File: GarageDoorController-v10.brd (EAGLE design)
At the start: 84.8 x 61 mm, 21 parts, among them IC1 ATMEGA328, IC2 TO-220, J1 ICSP, J2 DCJ0202, Q1 2N2222A, X1 Garage Door, X2 Reed Switch, X3 ETH SHLD, X4 ETH SHLD, Y1 16MHz

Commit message: GarageDoorController-v10.brd file should be ready for home fabrication.
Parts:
- moved J1 1.27 mm to (80.0, 25.4)
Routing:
- net +5V: track 150.7 -> 161.1 mm, vias 0 -> 1
- net N$17: track 0.00 -> 8.93 mm
- net N$10: track 0.00 -> 8.89 mm
- net N$9: track 0.00 -> 7.62 mm
- net N$8: track 0.00 -> 6.65 mm
- net GND: vias 0 -> 2
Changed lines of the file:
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@@
 <element name="D1" library="diode" package="DO41-10" value="1N4004" x="25.4" y="45.72"/>
 <element name="Q1" library="transistor-npn" package="TO18" value="2N2222A" x="29.21" y="38.1"/>
-<element name="J1" library="SparkFun-Connectors" package="2X3" value="ICSP" x="81.28" y="25.4" rot="R90"/>
+<element name="J1" library="SparkFun-Connectors" package="2X3" value="ICSP" x="80.01" y="25.4" rot="R90"/>
 <element name="LED1" library="led" package="LED5MM" value="RED" x="62.23" y="8.89" rot="R270"/>
 <element name="J2" library="con-jack" package="DCJ0202" value="DCJ0202" x="8.89" y="7.62" smashed="yes" rot="R270">
@@
 <wire x1="60.96" y1="58.42" x2="59.69" y2="60.325" width="0.6096" layer="16"/>
 <wire x1="59.69" y1="60.325" x2="34.29" y2="58.42" width="0.6096" layer="16"/>
-<wire x1="35.31" y1="58.17" x2="34.29" y2="58.42" width="0" layer="19" extent="16-16"/>
-<wire x1="48.26" y1="21.59" x2="50.8" y2="29.21" width="0" layer="19" extent="1-1"/>
-<wire x1="49.53" y1="4.064" x2="48.26" y2="21.59" width="0" layer="19" extent="1-1"/>
 <wire x1="3.81" y1="39.33" x2="20.32" y2="45.72" width="0.6096" layer="16"/>
 <wire x1="45.72" y1="21.59" x2="48.26" y2="21.59" width="0.6096" layer="16"/>
 <wire x1="50.8" y1="29.21" x2="50.8" y2="31.75" width="0.6096" layer="16"/>
-<wire x1="50.8" y1="31.75" x2="53.34" y2="34.29" width="0.6096" layer="16"/>
+<wire x1="50.8" y1="31.75" x2="52.07" y2="33.02" width="0.6096" layer="16"/>
+<wire x1="52.07" y1="33.02" x2="53.34" y2="34.29" width="0.6096" layer="16"/>
 <wire x1="53.34" y1="34.29" x2="58.42" y2="34.29" width="0.6096" layer="16"/>
+<wire x1="49.53" y1="4.064" x2="49.53" y2="1.27" width="0.6096" layer="16"/>
+<via x="52.07" y="33.02" extent="1-16" drill="1"/>
+<wire x1="48.26" y1="21.59" x2="48.26" y2="13.97" width="0.6096" layer="16"/>
+<wire x1="35.31" y1="58.17" x2="34.29" y2="58.42" width="0" layer="19" extent="16-16"/>
+<wire x1="48.26" y1="21.59" x2="50.8" y2="29.21" width="0" layer="19" extent="1-1"/>
+<wire x1="49.53" y1="4.064" x2="48.26" y2="13.97" width="0" layer="19" extent="16-16"/>
 </signal>
 <signal name="GND">
@@
 <wire x1="52.38" y1="46.68" x2="53.34" y2="45.72" width="0.6096" layer="16"/>
 <wire x1="53.34" y1="45.72" x2="53.34" y2="41.91" width="0.6096" layer="16"/>
-<wire x1="53.34" y1="41.91" x2="48.26" y2="29.21" width="0.6096" layer="16"/>
-<wire x1="50.8" y1="21.59" x2="55.88" y2="12.7" width="0.6096" layer="16"/>
+<wire x1="53.34" y1="41.91" x2="50.8" y2="35.56" width="0.6096" layer="16"/>
+<wire x1="50.8" y1="35.56" x2="48.26" y2="29.21" width="0.6096" layer="16"/>
+<wire x1="50.8" y1="21.59" x2="53.34" y2="17.145" width="0.6096" layer="16"/>
+<wire x1="53.34" y1="17.145" x2="55.88" y2="12.7" width="0.6096" layer="16"/>
 <wire x1="55.88" y1="12.7" x2="62.23" y2="13.97" width="0.6096" layer="16"/>
 <wire x1="62.23" y1="13.97" x2="66.04" y2="12.7" width="0.6096" layer="16"/>
 <wire x1="66.04" y1="12.7" x2="66.13769375" y2="8.1084625" width="0.6096" layer="16"/>
+<via x="50.8" y="35.56" extent="1-16" drill="1"/>
+<via x="53.34" y="17.145" extent="1-16" drill="1"/>
 <wire x1="50.8" y1="21.59" x2="48.26" y2="29.21" width="0" layer="19" extent="1-1"/>
 </signal>
@@
 <contactref element="J1" pad="3"/>
 <contactref element="IC1" pad="19"/>
-<wire x1="43.18" y1="21.59" x2="81.28" y2="27.94" width="0" layer="19" extent="1-1"/>
+<wire x1="80.01" y1="27.94" x2="82.55" y2="29.21" width="0.6096" layer="16"/>
+<wire x1="43.18" y1="21.59" x2="43.18" y2="17.78" width="0.6096" layer="16"/>
+<wire x1="43.18" y1="21.59" x2="80.01" y2="27.94" width="0" layer="19" extent="1-1"/>
 </signal>
 <signal name="N$9">
 <contactref element="J1" pad="1"/>
 <contactref element="IC1" pad="18"/>
-<wire x1="40.64" y1="21.59" x2="81.28" y2="25.4" width="0" layer="19" extent="1-1"/>
+<wire x1="80.01" y1="25.4" x2="80.01" y2="21.59" width="0.6096" layer="16"/>
+<wire x1="40.64" y1="21.59" x2="40.64" y2="17.78" width="0.6096" layer="16"/>
+<wire x1="40.64" y1="21.59" x2="80.01" y2="21.59" width="0" layer="19" extent="16-16"/>
 </signal>
 <signal name="N$10">
 <contactref element="J1" pad="4"/>
 <contactref element="IC1" pad="17"/>
-<wire x1="38.1" y1="21.59" x2="78.74" y2="27.94" width="0" layer="19" extent="1-1"/>
+<wire x1="77.47" y1="27.94" x2="72.39" y2="27.94" width="0.6096" layer="16"/>
+<wire x1="38.1" y1="21.59" x2="38.1" y2="17.78" width="0.6096" layer="16"/>
+<wire x1="38.1" y1="21.59" x2="72.39" y2="27.94" width="0" layer="19" extent="16-16"/>
 </signal>
 <signal name="N$11">
@@
 <contactref element="IC1" pad="16"/>
 <contactref element="X4" pad="2"/>
-<wire x1="35.56" y1="21.59" x2="58.46" y2="57.15" width="0" layer="19" extent="1-1"/>
+<wire x1="35.56" y1="21.59" x2="35.56" y2="17.78" width="0.6096" layer="16"/>
+<wire x1="58.46" y1="57.15" x2="53.34" y2="57.15" width="0.6096" layer="16"/>
+<wire x1="35.56" y1="21.59" x2="53.34" y2="57.15" width="0" layer="19" extent="16-16"/>
+</signal>
+<signal name="N$4">
+<via x="35.56" y="17.78" extent="1-16" drill="1"/>
+</signal>
+<signal name="N$18">
+<via x="38.1" y="17.78" extent="1-16" drill="1"/>
+</signal>
+<signal name="N$19">
+<via x="40.64" y="17.78" extent="1-16" drill="1"/>
+</signal>
+<signal name="N$20">
+<via x="43.18" y="17.78" extent="1-16" drill="1"/>
+</signal>
+<signal name="N$21">
+<via x="48.26" y="17.78" extent="1-16" drill="1"/>
+</signal>
+<signal name="N$22">
+<via x="80.01" y="21.59" extent="1-16" drill="1"/>
+</signal>
+<signal name="N$23">
+<via x="72.39" y="27.94" extent="1-16" drill="1"/>
+</signal>
+<signal name="N$24">
+<via x="82.55" y="29.21" extent="1-16" drill="1"/>
+</signal>
+<signal name="N$25">
+<via x="53.34" y="57.15" extent="1-16" drill="1"/>
+</signal>
+<signal name="N$26">
+<via x="49.53" y="1.27" extent="1-16" drill="1"/>
+</signal>
+<signal name="N$3">
+<via x="48.26" y="13.97" extent="1-16" drill="1"/>
 </signal>
 </signals>

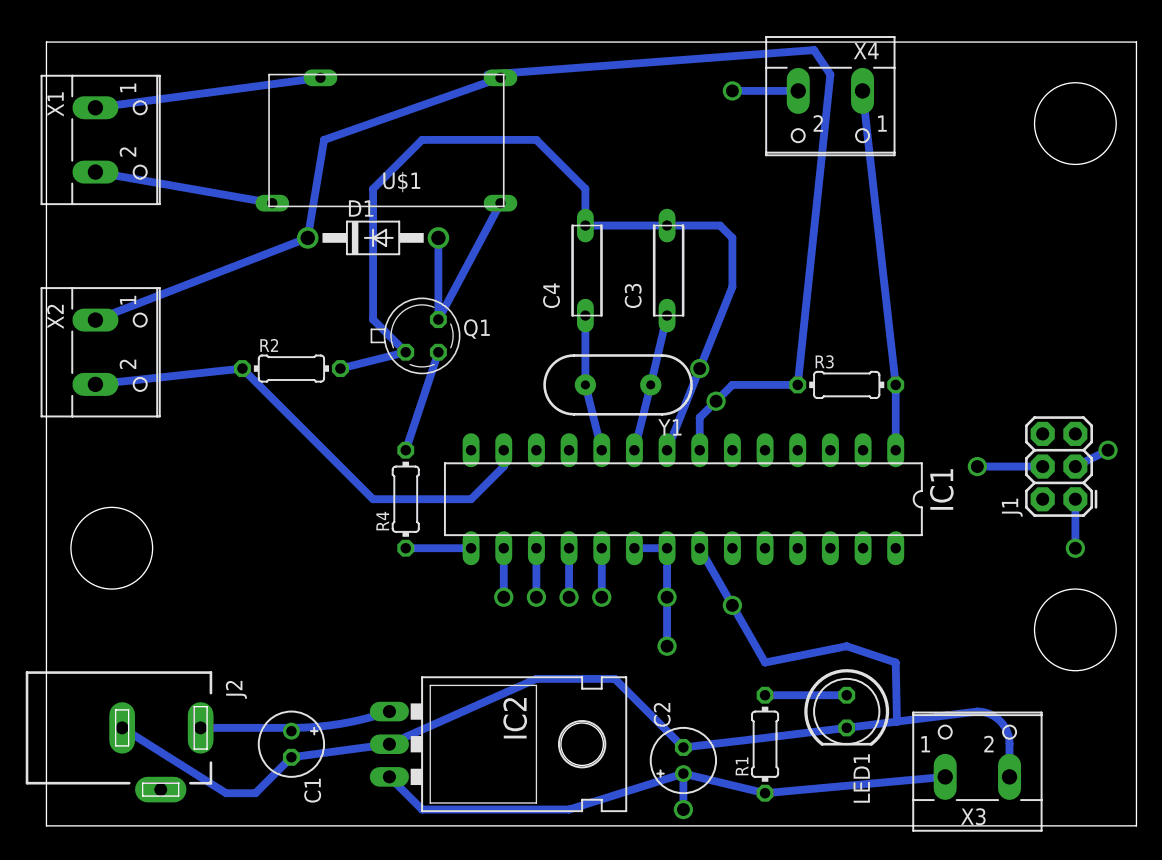
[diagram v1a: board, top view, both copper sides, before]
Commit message: Fixed the pin locations of the relay, added 'Thumbs.db' to .gitignore.
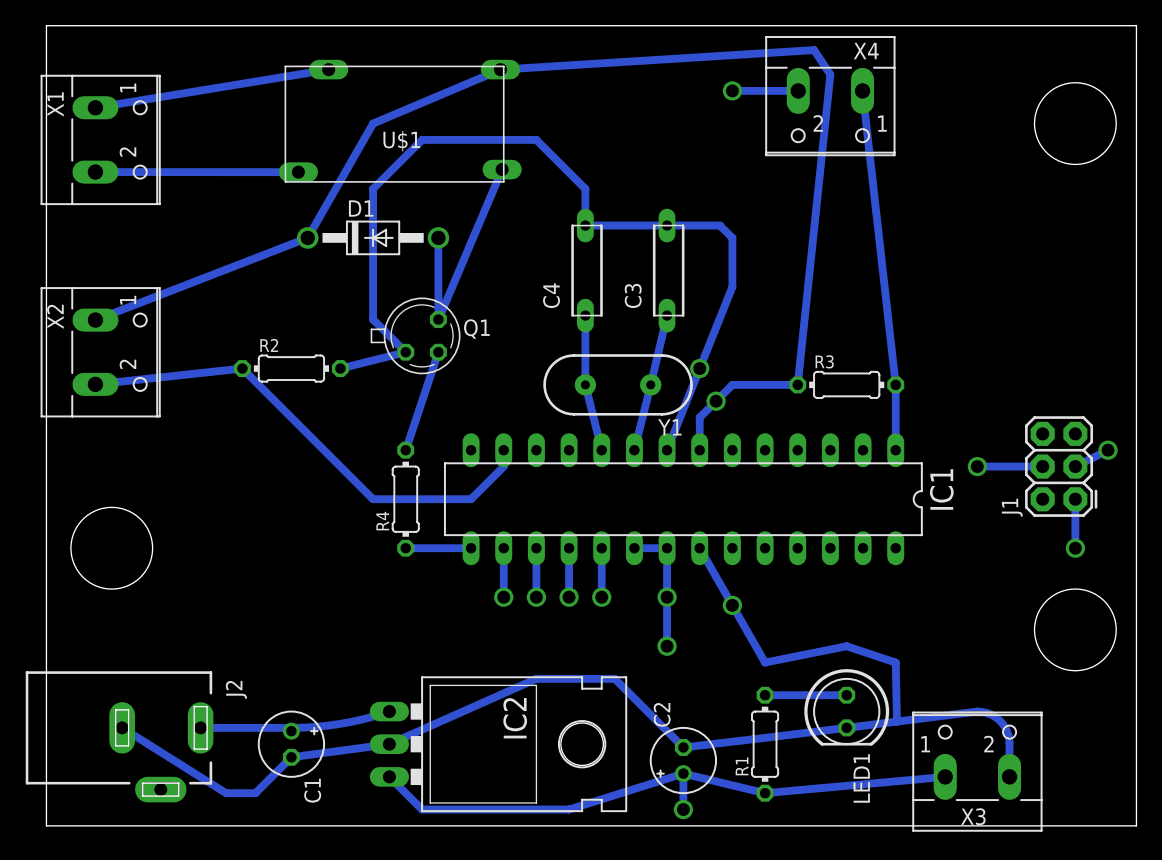
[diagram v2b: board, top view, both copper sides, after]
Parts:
- moved U$1 0.63 mm to (35.6, 59.1)
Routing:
- net N$13: track 16.6 -> 19.0 mm
- net +5V: track 161.1 -> 158.8 mm
- net N$14: track 14.0 -> 15.8 mm
- net N$16: track 17.7 -> 18.4 mm
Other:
- board size 84.8 x 61 mm -> 84.8 x 62.2 mm
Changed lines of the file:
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@@
 <plain>
 <wire x1="0" y1="0" x2="84.76" y2="0" width="0" layer="20"/>
-<wire x1="84.76" y1="0" x2="84.76" y2="60.95" width="0" layer="20"/>
-<wire x1="84.76" y1="60.95" x2="0" y2="60.95" width="0" layer="20"/>
-<wire x1="0" y1="60.95" x2="0" y2="0" width="0" layer="20"/>
+<wire x1="84.76" y1="0" x2="84.76" y2="62.22" width="0" layer="20"/>
+<wire x1="84.76" y1="62.22" x2="0" y2="62.22" width="0" layer="20"/>
+<wire x1="0" y1="62.22" x2="0" y2="0" width="0" layer="20"/>
 <hole x="80.01" y="54.61" drill="6.35"/>
 <hole x="80.01" y="15.24" drill="6.35"/>
@@
 <element name="C3" library="domiflichi" package="1440PH" value="1440PH" x="48.26" y="43.18"/>
 <element name="C4" library="domiflichi" package="1440PH" value="1440PH" x="41.91" y="43.18"/>
-<element name="U$1" library="domiflichi" package="PB874" value="PB874FORMA" x="35.56" y="58.42" rot="R180"/>
+<element name="U$1" library="domiflichi" package="PB874" value="PB874FORMA" x="35.56" y="59.055" rot="R180"/>
 <element name="X3" library="con-wago-500" package="W237-102" value="ETH SHLD" x="72.39" y="5.08" smashed="yes">
 <attribute name="OC_NEWARK" value="70K9898" x="90.17" y="-45.72" size="1.778" layer="27" display="off"/>
@@
 <wire x1="40.64" y1="1.27" x2="49.53" y2="4.064" width="0.6096" layer="16"/>
 <wire x1="49.53" y1="4.064" x2="55.88" y2="2.54" width="0.6096" layer="16"/>
-<wire x1="35.31" y1="58.17" x2="21.59" y2="53.34" width="0.6096" layer="16"/>
-<wire x1="21.59" y1="53.34" x2="20.32" y2="45.72" width="0.6096" layer="16"/>
+<wire x1="25.4" y1="54.61" x2="20.32" y2="45.72" width="0.6096" layer="16"/>
 <wire x1="58.42" y1="34.29" x2="60.96" y2="58.42" width="0.6096" layer="16"/>
 <wire x1="60.96" y1="58.42" x2="59.69" y2="60.325" width="0.6096" layer="16"/>
-<wire x1="59.69" y1="60.325" x2="34.29" y2="58.42" width="0.6096" layer="16"/>
 <wire x1="3.81" y1="39.33" x2="20.32" y2="45.72" width="0.6096" layer="16"/>
 <wire x1="45.72" y1="21.59" x2="48.26" y2="21.59" width="0.6096" layer="16"/>
@@
 <via x="52.07" y="33.02" extent="1-16" drill="1"/>
 <wire x1="48.26" y1="21.59" x2="48.26" y2="13.97" width="0.6096" layer="16"/>
-<wire x1="35.31" y1="58.17" x2="34.29" y2="58.42" width="0" layer="19" extent="16-16"/>
+<wire x1="35.31" y1="58.805" x2="25.4" y2="54.61" width="0.6096" layer="16"/>
 <wire x1="48.26" y1="21.59" x2="50.8" y2="29.21" width="0" layer="19" extent="1-1"/>
 <wire x1="49.53" y1="4.064" x2="48.26" y2="13.97" width="0" layer="19" extent="16-16"/>
+<wire x1="35.31" y1="58.805" x2="59.69" y2="60.325" width="0.6096" layer="16"/>
 </signal>
 <signal name="GND">
@@
 <contactref element="U$1" pad="1"/>
 <wire x1="30.48" y1="45.72" x2="30.48" y2="39.37" width="0.6096" layer="16"/>
-<wire x1="35.31" y1="48.42" x2="30.48" y2="39.37" width="0.6096" layer="16"/>
+<wire x1="35.437" y1="51.03621875" x2="30.48" y2="39.37" width="0.6096" layer="16"/>
 </signal>
 <signal name="N$15">
@@
 <contactref element="U$1" pad="4"/>
 <contactref element="X1" pad="2"/>
-<wire x1="3.81" y1="50.84" x2="17.56" y2="48.42" width="0.6096" layer="16"/>
+<wire x1="3.81" y1="50.84" x2="19.593559375" y2="50.83301875" width="0.6096" layer="16"/>
 </signal>
 <signal name="N$16">
 <contactref element="U$1" pad="3"/>
 <contactref element="X1" pad="1"/>
-<wire x1="3.81" y1="55.84" x2="21.31" y2="58.17" width="0.6096" layer="16"/>
+<wire x1="3.81" y1="55.84" x2="21.9456" y2="58.805" width="0.6096" layer="16"/>
 </signal>
 <signal name="N$17">

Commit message: Modified GarageDoorController-v10.brd file: Shrunk overall board size, moving parts around, closer together.
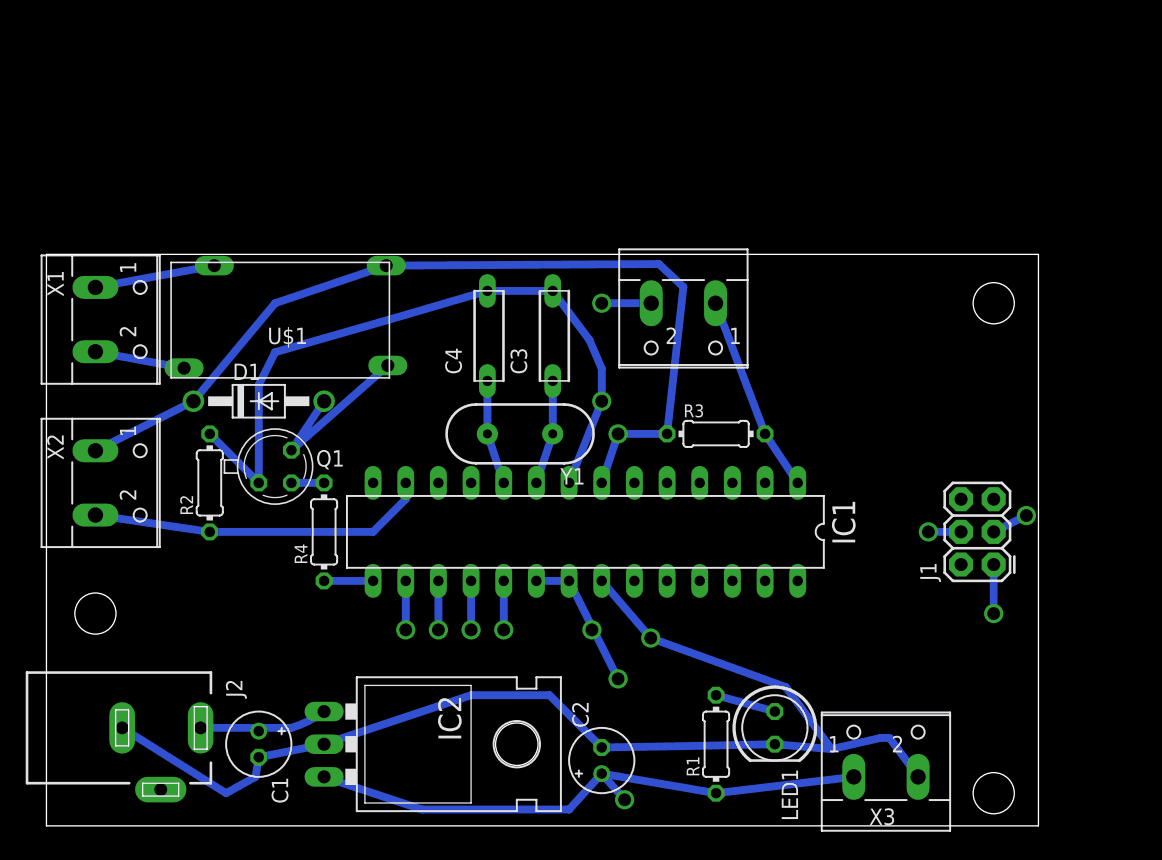
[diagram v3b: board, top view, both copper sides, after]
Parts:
- moved X4 20.1 mm to (49.5, 39.4)
- moved U$1 17.6 mm to (26.7, 43.8)
- moved D1 15.5 mm to (16.5, 33.0)
- moved Q1 15.3 mm to (17.8, 27.9)
- moved X1 14.0 mm to (5.08, 39.4)
- moved R2 10.9 mm to (12.7, 26.7), turned to 90 degrees
- moved R3 10.9 mm to (52.1, 30.5)
- moved C3 10.2 mm to (39.4, 38.1)
- moved X2 10.2 mm to (5.08, 26.7)
- moved C4 9.16 mm to (34.3, 38.1)
- moved Y1 8.52 mm to (36.8, 30.5)
- moved J1 8.13 mm to (73.7, 20.3)
- moved IC1 8.03 mm to (41.9, 22.9)
- moved X3 7.11 mm to (65.3, 5.08)
- moved R4 6.84 mm to (21.6, 22.9)
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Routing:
- net +5V: track 158.8 -> 127.5 mm
- net GND: track 174.9 -> 146.7 mm
- net N$7: track 28.1 -> 15.4 mm
- net N$12: track 38.3 -> 26.5 mm
- net N$16: track 18.4 -> 9.40 mm
- net N$14: track 15.8 -> 7.01 mm
- net N$11: track 8.03 -> 2.54 mm
- net N$5: track 14.8 -> 9.90 mm
- net N$13: track 19.0 -> 14.6 mm
- net N$2: track 10.8 -> 8.14 mm
- net N$10: track 8.89 -> 6.35 mm
- net N$1: track 10.6 -> 8.14 mm
- net N$6: track 6.35 -> 4.75 mm
- net N$15: track 5.08 -> 3.81 mm
- net N$17: track 8.93 -> 7.66 mm
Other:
- board size 84.8 x 62.2 mm -> 77.1 x 44.4 mm
